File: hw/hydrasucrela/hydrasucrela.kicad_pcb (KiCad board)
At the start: 2 copper layers, 100 x 100 mm, 5 parts, among them U2 ECP5U_25_CABGA381, U3 TLV62569DRL, U4 NCP115CMX250TCG, U5 XUY73, U6 MCP23S08-E/SO

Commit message: hw: update kicad footprints and symbols
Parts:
- removed U2: ECP5U_25_CABGA381, Package_BGA:Lattice_caBGA-381_17.0x17.0mm_Layout20x20_P0.8mm_Ball0.4mm_Pad0.4mm_NSMD
- added C1, C3, C4: 10uF, Capacitor_SMD:C_0603_1608Metric_Pad1.08x0.95mm_HandSolder, F.Cu at (141.1, 70.4)
- added C2: 10pF, Capacitor_SMD:C_0603_1608Metric_Pad1.08x0.95mm_HandSolder, F.Cu at (141.1, 70.4)
- added C5: 4.7uF, Capacitor_SMD:C_0603_1608Metric_Pad1.08x0.95mm_HandSolder, F.Cu at (141.1, 70.4)
- added C6: 0.01uF, Capacitor_SMD:C_0603_1608Metric_Pad1.08x0.95mm_HandSolder, F.Cu at (141.1, 70.4)
- added J1: Conn_02x20_Odd_Even, Connector_Harwin:Harwin_M20-7812045_2x20_P2.54mm_Vertical, F.Cu at (205.3, 104.8)
- added J2: Conn_02x05_Odd_Even, Connector_Harwin:Harwin_M20-7810545_2x05_P2.54mm_Vertical, F.Cu at (138.1, 130.0)
- added J3: Conn_02x05_Odd_Even, Connector_Harwin:Harwin_M20-7810545_2x05_P2.54mm_Vertical, F.Cu at (163.0, 76.0)
- added J4: Conn_01x05, Connector_PinSocket_2.54mm:PinSocket_1x05_P2.54mm_Vertical, F.Cu at (141.1, 70.4)
- added L1: 2.2uH, Inductor_SMD:L_0603_1608Metric_Pad1.05x0.95mm_HandSolder, F.Cu at (141.1, 70.4)
- added Q1: MMBTA06, Package_TO_SOT_SMD:SOT-23, F.Cu at (123.0, 142.0)
- added R1: 10k, Resistor_SMD:R_0603_1608Metric_Pad0.98x0.95mm_HandSolder, F.Cu at (141.1, 70.4)
- added R2: 100k, Resistor_SMD:R_0603_1608Metric_Pad0.98x0.95mm_HandSolder, F.Cu at (141.1, 70.4)
- added R3: 120k, Resistor_SMD:R_0603_1608Metric_Pad0.98x0.95mm_HandSolder, F.Cu at (141.1, 70.4)
- added R4, R5, R6: 4.7k, Resistor_SMD:R_0603_1608Metric_Pad0.98x0.95mm_HandSolder, F.Cu at (141.1, 70.4)
- added U1: ECP5U_25_CABGA381, Package_BGA:Lattice_caBGA-381_17.0x17.0mm_Layout20x20_P0.8mm_Ball0.4mm_Pad0.4mm_NSMD, F.Cu at (165.9, 104.7)
- moved U4 101.2 mm to (204.0, 56.0)
- moved U5 92.7 mm to (206.0, 63.0)
- moved U6 60.1 mm to (177.0, 146.0)
- moved U3 19.6 mm to (124.0, 147.0)
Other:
- copper layers 2 -> 4

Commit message: Update HydraSucreLA PCB
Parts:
- added J5: Conn_02x20_Top_Bottom, Library:probe_connector, F.Cu at (11.9, 43.1)
- C2, C5, C6, L1, Q1, R1, R2, R3, R5, R6, U3, U4, U6: moved to B.Cu
- moved U4 167.2 mm to (36.9, 58.4), turned to 180 degrees
- moved U5 162.0 mm to (47.5, 29.2), turned to -90 degrees
- moved U6 156.8 mm to (48.1, 56.8), turned to 180 degrees
- moved J1 156.1 mm to (62.6, 41.5), turned to 0 degrees
- moved J2 148.1 mm to (41.5, 17.7), turned to -90 degrees
- moved U3 141.9 mm to (24.5, 45.8), turned to 180 degrees
- moved U1 136.5 mm to (44.6, 42.1)
- moved C1 128.5 mm to (24.0, 17.5)
- moved C4 123.9 mm to (27.9, 19.9)
- moved R4 122.8 mm to (18.4, 64.4), turned to 180 degrees
- moved C3 122.4 mm to (27.9, 23.9)
- moved J3 121.9 mm to (41.5, 66.5), turned to -90 degrees
- moved L1 118.8 mm to (25.3, 43.8)
- moved R2 118.6 mm to (26.9, 38.3), turned to 180 degrees
- moved C2 118.4 mm to (24.7, 48.8), turned to 180 degrees
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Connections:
- J1 pad 10: HD23 -> HD12
- J1 pad 11: HD20 -> HD10
- J1 pad 12: HD21 -> HD8
- J1 pad 13: HD18 -> HD6
- J1 pad 14: HD19 -> HD4
- J1 pad 15: HD16 -> HD2
- J1 pad 16: HD17 -> HD0
- J1 pad 17: HD14 -> HTACK
- J1 pad 18: HD15 -> HRCLK
- J1 pad 19: HD12 -> HTRDY
- J1 pad 2: HD31 -> HD28
- J1 pad 20: HD13 -> HTCLK
- J1 pad 21: HD10 -> HD31
- J1 pad 22: HD11 -> HD29
- J1 pad 23: HD8 -> HD27
- J1 pad 24: HD9 -> HD25
- J1 pad 25: HD6 -> HD23
- J1 pad 26: HD7 -> HD21
- J1 pad 27: HD4 -> HD19
- J1 pad 28: HD5 -> HD17
- J1 pad 29: HD2 -> HD15
- J1 pad 3: HD28 -> HD26
- J1 pad 30: HD3 -> HD13
- J1 pad 31: HD0 -> HD11
- J1 pad 32: HD1 -> HD9
- J1 pad 33: HTACK -> HD7
- J1 pad 34: HRVLD -> HD5
- J1 pad 35: HRCLK -> HD3
- J1 pad 36: HRACT -> HD1
- J1 pad 37: HTRDY -> HRVLD
- J1 pad 38: HTVLD -> HRACT
- J1 pad 39: HTCLK -> HTVLD
- J1 pad 4: HD29 -> HD24
- J1 pad 5: HD26 -> HD22
- J1 pad 6: HD27 -> HD20
- J1 pad 7: HD24 -> HD18
- J1 pad 8: HD25 -> HD16
- J1 pad 9: HD22 -> HD14
- J2 pad 2: GND -> SCS0
- J2 pad 3: SCS0 -> MOSI0
- J2 pad 4: SCK0 -> GND
- J2 pad 5: MOSI0 -> GND
- J2 pad 6: MISO0 -> GND
- J2 pad 7: GND -> SCK0
- J2 pad 8: P5.0V -> MISO0
- J2 pad 9: GND -> P5.0V
- J3 pad 2: 3V3_IN -> GND
- J3 pad 4: GND -> RXD_1
- J3 pad 6: GND -> 3V3_IN
- J3 pad 7: RXD_1 -> GND
- J3 pad 8: TXD_1 -> GND
- J3 pad 9: GND -> TXD_1
- U1 pad A2: Probe_8 -> Probe_0
- U1 pad A4: Probe_0 -> Probe_1
- U1 pad A5: Probe_1 -> unconnected-(U1G-PL2B/-/HS/LDQ8-PadA5)
- U1 pad B1: Probe_9 -> Probe_2
- U1 pad C1: Probe_10 -> Probe_4
- U1 pad C18: HD0 -> unconnected-(U1D-PR2A/+/HS/RDQ8-PadC18)
- U1 pad C20: HD16 -> HD31
- U1 pad C4: Probe_2 -> Probe_5
- U1 pad D1: Probe_11 -> unconnected-(U1G-PL17B/-/HS/LDQ20-PadD1)
- U1 pad D17: HD1 -> HD30
- U1 pad D18: HD4 -> HD28
- U1 pad D19: HD17 -> HD29
- U1 pad D20: HD18 -> HD27
- U1 pad D5: Probe_5 -> unconnected-(U1G-PL8B/-/HS/LDQSN8-PadD5)
- U1 pad E16: HD2 -> HD22
- U1 pad E17: HD5 -> HD26
- U1 pad E18: HD6 -> HD24
- U1 pad E19: HD19 -> HD25
- U1 pad E20: HD20 -> HD23
- U1 pad E3: Probe_7 -> Probe_6
- U1 pad E4: Probe_4 -> unconnected-(U1G-PL8A/+/HS/LDQS8-PadE4)
- U1 pad F1: Probe_1 -> unconnected-(U1F-PL26B/-/PCLKC6_1/HS/LDQ32-PadF1)
- U1 pad F16: HD3 -> HD20
- U1 pad F17: HD8 -> HD18
- U1 pad F18: HD7 -> HD16
- U1 pad F20: HD22 -> HD19
- U1 pad F3: Probe_15 -> unconnected-(U1G-PL23B/-/PCLKC7_1/HS/LDQ20-PadF3)
- U1 pad F4: Probe_6 -> unconnected-(U1G-PL11A/+/HS/LDQ8-PadF4)
- U1 pad G16: HD10 -> HD14
- U1 pad G18: HD9 -> HD12
- U1 pad G19: HD24 -> HD17
- U1 pad G2: Probe_0 -> Probe_7
- U1 pad G20: HD23 -> HD15
- U1 pad G3: Probe_14 -> unconnected-(U1G-PL23A/+/PCLKT7_1/HS/LDQ20-PadG3)
- U1 pad G5: Probe_13 -> unconnected-(U1G-PL20B/-/HS/LDQSN20-PadG5)
- U1 pad H16: HD11 -> HD6
- U1 pad H17: HD13 -> HD8
- U1 pad H18: HD12 -> HD10
- U1 pad H20: HD25 -> HD13
- U1 pad H4: Probe_12 -> unconnected-(U1G-PL20A/+/GR_PCLK7_1/HS/LDQS20-PadH4)
- U1 pad J1: Probe_5 -> Probe_8
- U1 pad J16: HD15 -> HD2
- U1 pad J17: HD14 -> HD4
- U1 pad J18: HD26 -> HD0
- U1 pad J19: HD28 -> HD11
- U1 pad J20: HD30 -> HD9
- U1 pad J4: Probe_2 -> unconnected-(U1F-PL29A/+/GR_PCLK6_0/HS/LDQ32-PadJ4)
- U1 pad J5: Probe_3 -> unconnected-(U1F-PL29B/-/HS/LDQ32-PadJ5)
- U1 pad K18: HD27 -> HTACK
- U1 pad K19: HD29 -> HD7
- U1 pad K2: Probe_4 -> Probe_9
- U1 pad K20: HD31 -> HD5
- U1 pad K4: Probe_6 -> unconnected-(U1F-PL35A/+/HS/LDQ32-PadK4)
- U1 pad K5: Probe_7 -> unconnected-(U1F-PL35B/-/VREF1_6/HS/LDQ32-PadK5)
- U1 pad L16: HTRDY -> HTCLK
- U1 pad L17: HRCLK -> HTRDY
- U1 pad L18: HRACT -> HRCLK
- U1 pad L19: HTREQ -> HD3
- U1 pad L20: HTACK -> HD1
- U1 pad M1: Probe_13 -> Probe_10
- U1 pad M17: TXD_1 -> HTVLD
- U1 pad M18: HRVLD -> unconnected-(U1E-PR29D/-/RDQ32-PadM18)
- U1 pad M19: HTVLD -> HRVLD
- U1 pad M20: HTCLK -> HRACT
- U1 pad M4: Probe_8 -> unconnected-(U1F-PL38A/+/HS/LDQ44-PadM4)
- U1 pad N16: RXD_1 -> HTREQ
- U1 pad N3: Probe_10 -> Probe_15
- U1 pad N5: Probe_9 -> unconnected-(U1F-PL38B/-/HS/LDQ44-PadN5)
- U1 pad P1: Probe_14 -> Probe_13
- U1 pad P2: Probe_15 -> Probe_14
- U1 pad R1: unconnected-(U1H-PB4A/+/D7/IO7-PadR1) -> RXD_1
- U1 pad T1: unconnected-(U1H-PB4B/-/D6/IO6-PadT1) -> TXD_1
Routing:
- net GND: track 0.00 -> 64.6 mm, vias 0 -> 35
- net P5.0V: track 0.00 -> 45.5 mm, vias 0 -> 1
- net 3V3_IN: track 0.00 -> 39.4 mm, vias 0 -> 9
- net P1.1V: track 0.00 -> 37.4 mm, vias 0 -> 19
- net HTREQ: track 0.00 -> 33.9 mm, vias 0 -> 2
- net Probe_5: track 0.00 -> 32.0 mm
- net Probe_15: track 0.00 -> 32.0 mm
- net Probe_1: track 0.00 -> 32.0 mm
- net Probe_2: track 0.00 -> 32.0 mm
- net Net-(U3-FB): track 0.00 -> 31.9 mm, vias 0 -> 2
- net Probe_3: track 0.00 -> 31.9 mm
- net Probe_14: track 0.00 -> 31.9 mm
- net Probe_12: track 0.00 -> 31.9 mm
- net Probe_6: track 0.00 -> 31.9 mm
- net Probe_13: track 0.00 -> 31.9 mm
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- added copper zone on F.Cu, net 3V3_IN
- added copper zone on F.Cu, net GND
- added copper zone on In1.Cu, net GND
- added copper zone on F.Cu, net P1.1V
- added copper zone on F.Cu, net P1.8V
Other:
- board size 100 x 100 mm -> 60 x 60 mm

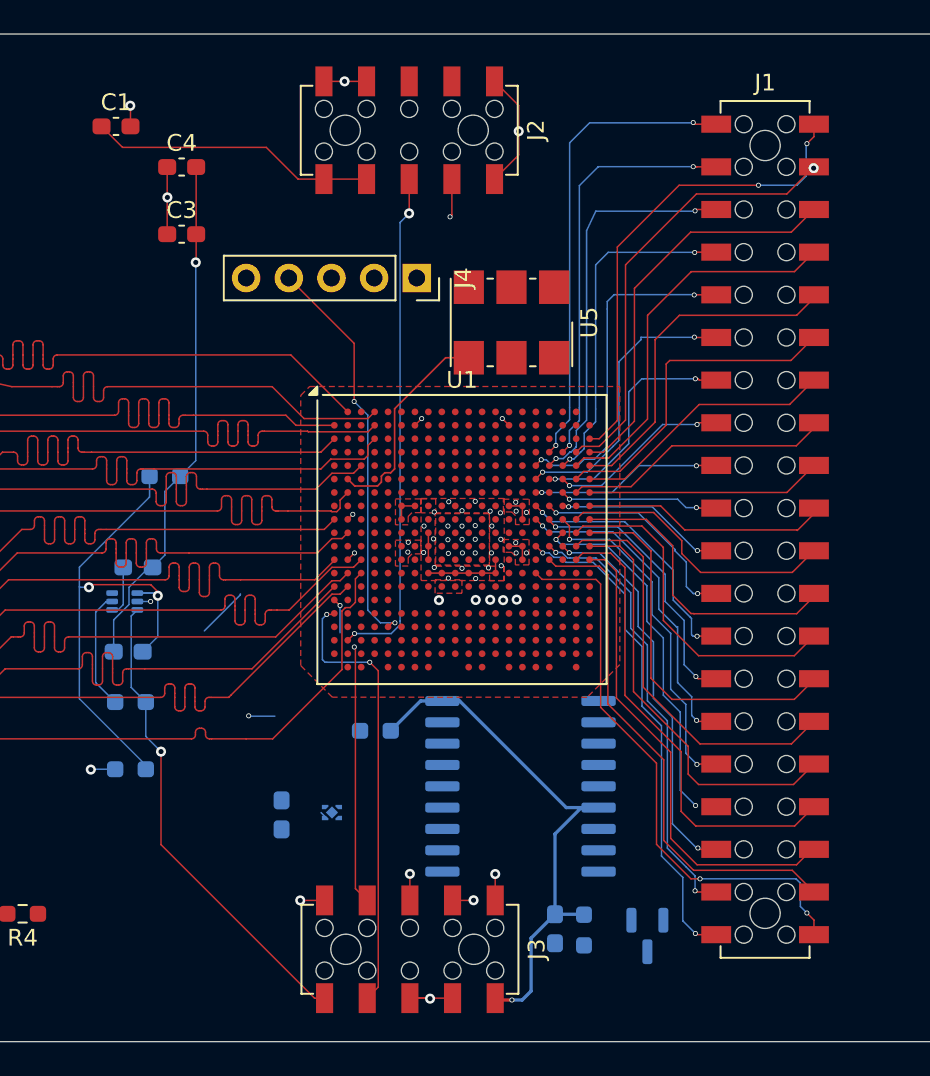
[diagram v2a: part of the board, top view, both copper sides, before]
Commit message: update PCB with good connector placements
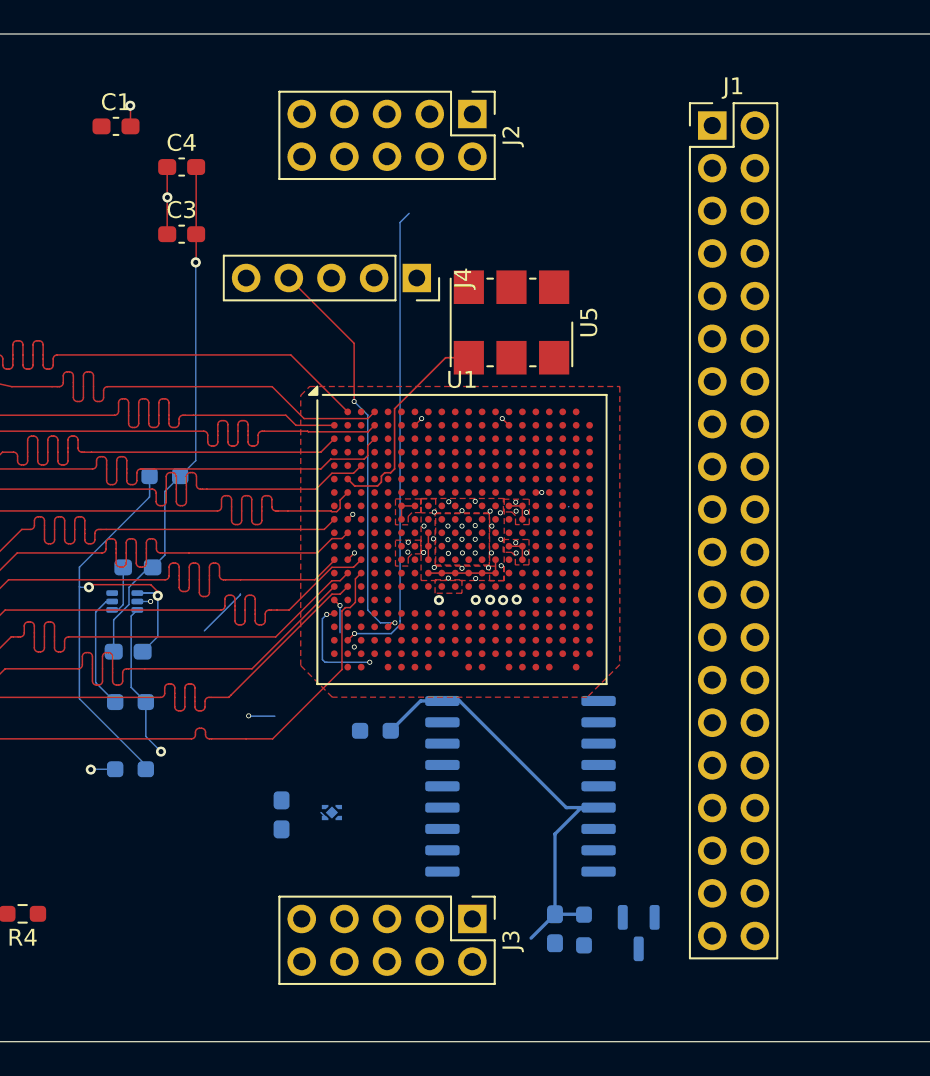
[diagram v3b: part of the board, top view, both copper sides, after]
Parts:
- J1: value Conn_02x20_Odd_Even -> Yxcon P125-1220A0BS116A1; footprint Connector_Harwin:Harwin_M20-7812045_2x20_P2.54mm_Vertical -> Connector_PinHeader_2.54mm:PinHeader_2x20_P2.54mm_Vertical
- J2, J3: value Conn_02x05_Odd_Even -> Megastar ZX-PZ2.54-2-5PZZ; footprint Connector_Harwin:Harwin_M20-7810545_2x05_P2.54mm_Vertical -> Connector_PinHeader_2.54mm:PinHeader_2x05_P2.54mm_Vertical
- moved J1 24.3 mm to (59.5, 17.4)
- moved J3 4.13 mm to (45.2, 64.7)
- moved J2 3.88 mm to (45.2, 16.8)
- moved Q1 0.54 mm to (55.1, 65.5)
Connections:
- J1 pad 10: HD12 -> HD23
- J1 pad 11: HD10 -> HD20
- J1 pad 12: HD8 -> HD21
- J1 pad 13: HD6 -> HD18
- J1 pad 14: HD4 -> HD19
- J1 pad 15: HD2 -> HD16
- J1 pad 16: HD0 -> HD17
- J1 pad 17: HTACK -> HD14
- J1 pad 18: HRCLK -> HD15
- J1 pad 19: HTRDY -> HD12
- J1 pad 2: HD28 -> HD31
- J1 pad 20: HTCLK -> HD13
- J1 pad 21: HD31 -> HD10
- J1 pad 22: HD29 -> HD11
- J1 pad 23: HD27 -> HD8
- J1 pad 24: HD25 -> HD9
- J1 pad 25: HD23 -> HD6
- J1 pad 26: HD21 -> HD7
- J1 pad 27: HD19 -> HD4
- J1 pad 28: HD17 -> HD5
- J1 pad 29: HD15 -> HD2
- J1 pad 3: HD26 -> HD28
- J1 pad 30: HD13 -> HD3
- J1 pad 31: HD11 -> HD0
- J1 pad 32: HD9 -> HD1
- J1 pad 33: HD7 -> HTACK
- J1 pad 34: HD5 -> HRVLD
- J1 pad 35: HD3 -> HRCLK
- J1 pad 36: HD1 -> HRACT
- J1 pad 37: HRVLD -> HTRDY
- J1 pad 38: HRACT -> HTVLD
- J1 pad 39: HTVLD -> HTCLK
- J1 pad 4: HD24 -> HD29
- J1 pad 5: HD22 -> HD26
- J1 pad 6: HD20 -> HD27
- J1 pad 7: HD18 -> HD24
- J1 pad 8: HD16 -> HD25
- J1 pad 9: HD14 -> HD22
- J2 pad 2: SCS0 -> GND
- J2 pad 3: MOSI0 -> SCS0
- J2 pad 4: GND -> SCK0
- J2 pad 5: GND -> MOSI0
- J2 pad 6: GND -> MISO0
- J2 pad 7: SCK0 -> GND
- J2 pad 8: MISO0 -> P5.0V
- J2 pad 9: P5.0V -> GND
- J3 pad 2: GND -> 3V3_IN
- J3 pad 4: RXD_1 -> GND
- J3 pad 6: 3V3_IN -> GND
- J3 pad 7: GND -> RXD_1
- J3 pad 8: GND -> TXD_1
- J3 pad 9: TXD_1 -> GND
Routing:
- net P5.0V: track 45.5 -> 9.33 mm
- net HTREQ: track 33.9 -> 0.00 mm, vias 2 -> 0
- net HTVLD: track 31.3 -> 0.00 mm
- net HTCLK: track 29.7 -> 0.01 mm, vias 2 -> 0
- net HD31: track 28.7 -> 0.00 mm, vias 2 -> 0
- net HRACT: track 28.7 -> 0.00 mm
- net HD30: track 28.2 -> 0.00 mm, vias 2 -> 0
- net HRVLD: track 28.1 -> 0.00 mm
- net HD29: track 26.6 -> 0.00 mm, vias 1 -> 0
- net HTRDY: track 26.6 -> 0.02 mm, vias 2 -> 0
- net HD1: track 25.3 -> 0.00 mm
- net HD28: track 24.9 -> 0.00 mm, vias 2 -> 0
- net HD3: track 24.4 -> 0.00 mm
- net HD27: track 24.0 -> 0.00 mm
- net HD26: track 23.7 -> 0.02 mm, vias 2 -> 0
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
